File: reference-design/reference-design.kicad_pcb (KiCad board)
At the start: 2 copper layers, 12 x 20.6 mm, 21 parts

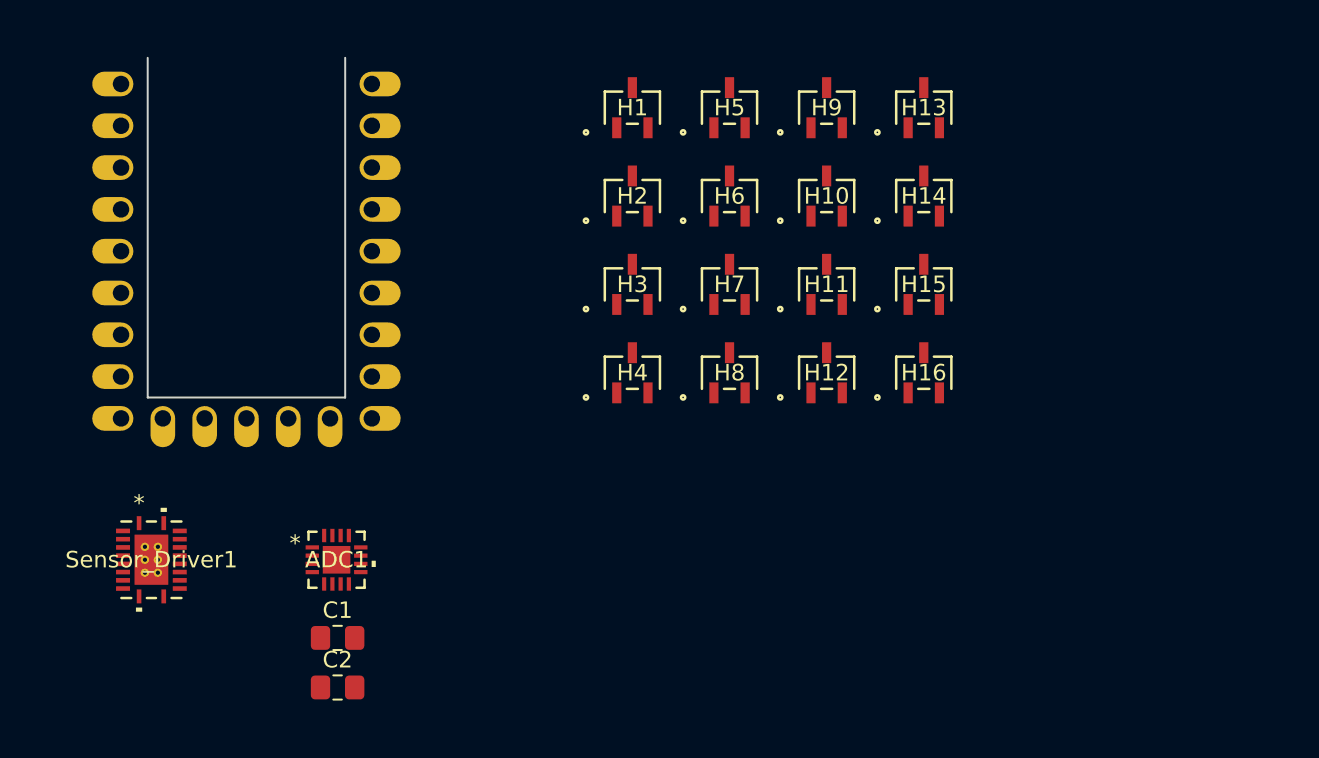
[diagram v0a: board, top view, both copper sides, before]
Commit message: associate 3d models for pcb preview
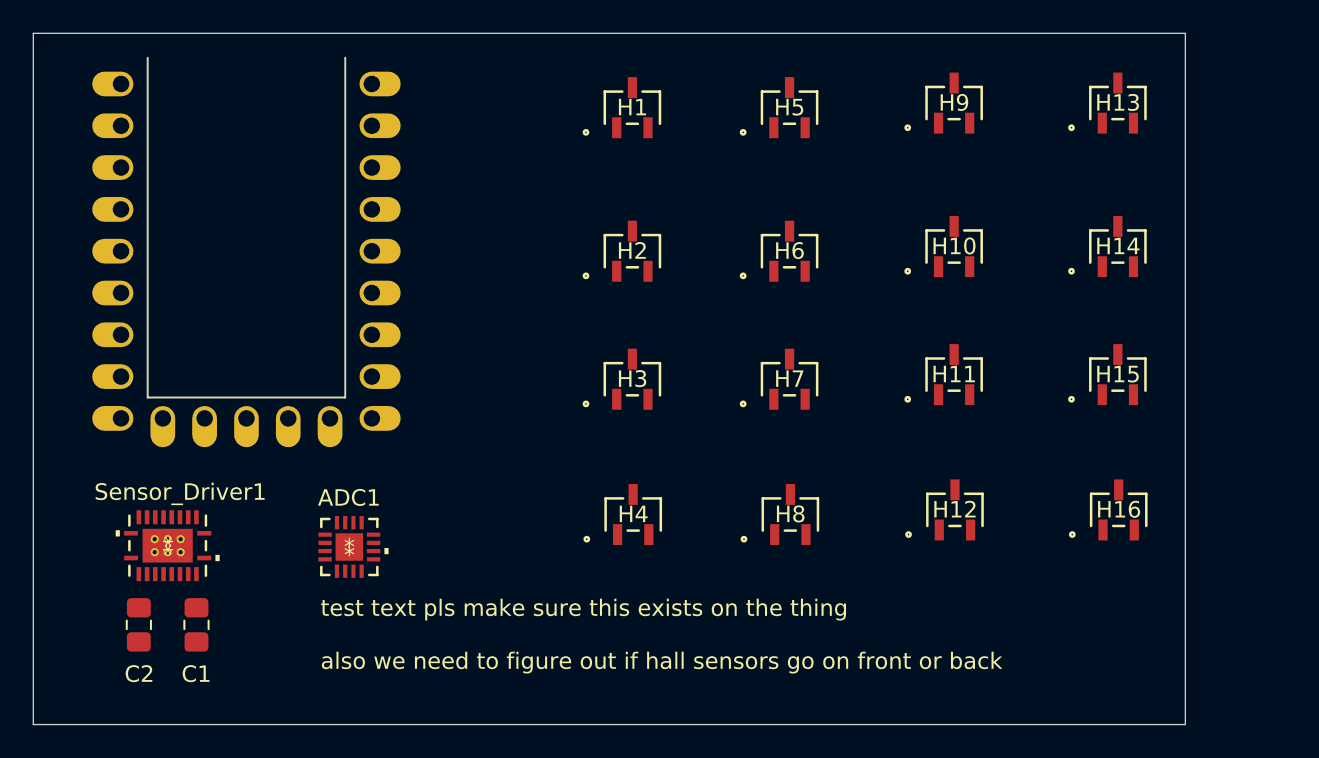
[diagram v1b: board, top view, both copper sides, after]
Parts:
- moved H16 14.5 mm to (78.5, 41.2)
- moved H15 13.0 mm to (78.5, 33.0)
- moved C2 12.7 mm to (19.0, 48.2), turned to 90 degrees
- moved H14 12.2 mm to (78.5, 25.2)
- moved H13 11.8 mm to (78.5, 16.5)
- moved H12 11.4 mm to (68.5, 41.2)
- moved H11 9.49 mm to (68.5, 33.0)
- moved H8 9.37 mm to (58.5, 41.5)
- moved H4 8.61 mm to (49.0, 41.5)
- moved C1 8.61 mm to (22.5, 48.2), turned to 90 degrees
- moved H10 8.33 mm to (68.5, 25.2)
- moved H9 7.75 mm to (68.5, 16.5)
- moved H7 6.82 mm to (58.5, 33.3)
- moved H3 5.76 mm to (49.0, 33.3)
- moved H6 4.95 mm to (58.5, 25.5)
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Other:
- board size 12 x 20.6 mm -> 70 x 42 mm
- board text added: "test text pls make sure this exists on the thing also we need to figure out if hall sensors go on front or back"

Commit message: SCH and PCB cleanup
- Ran ERC
- Added NCs to unused pins
- Fixed unconnected output pin on one of the sensors
- Cleaned up expected violations
- Rearranged sensors on PCB to match the pattern on the schematic
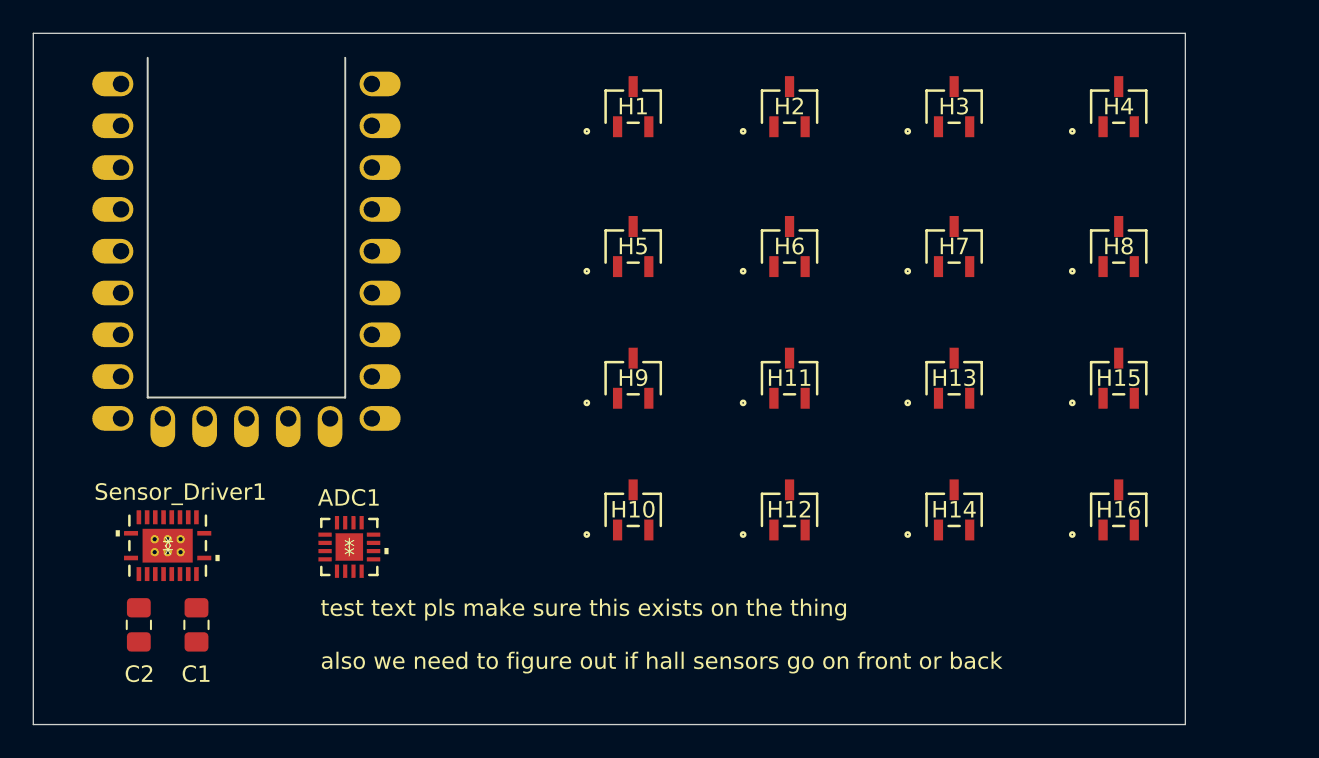
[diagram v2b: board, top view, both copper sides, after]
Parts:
- moved H4 38.5 mm to (78.5, 16.7)
- moved H8 25.8 mm to (78.5, 25.2)
- moved H9 25.7 mm to (49.0, 33.2)
- moved H3 25.6 mm to (68.5, 16.7)
- moved H10 25.2 mm to (49.0, 41.2)
- moved H13 19.5 mm to (68.5, 33.2)
- moved H14 18.8 mm to (68.5, 41.2)
- moved H2 13.0 mm to (58.5, 16.7)
- moved H7 12.8 mm to (68.5, 25.2)
- moved H5 12.7 mm to (49.0, 25.2)
- moved H12 10.0 mm to (58.5, 41.2)
- moved H11 10.0 mm to (58.5, 33.2)
- moved H6 0.28 mm to (58.5, 25.2)
- moved H15 0.22 mm to (78.5, 33.2)
- moved H1 0.08 mm to (49.0, 16.7)
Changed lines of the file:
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@@
 			(psa4output no)
 			(plot_black_and_white yes)
-			(plotinvisibletext no)
 			(sketchpadsonfab no)
 			(plotpadnumbers no)
@@
 	(footprint "AH49FNTR_G1:SC59_DIO"
 		(layer "F.Cu")
-		(at 49 41.5)
+		(at 78.5 16.7192)
 		(tags "AH49FNTR-G1 ")
 		(property "Reference" "H4"
@@
 	(footprint "AH49FNTR_G1:SC59_DIO"
 		(layer "F.Cu")
-		(at 58.5 33.2808)
+		(at 68.5 25.2192)
 		(tags "AH49FNTR-G1 ")
 		(property "Reference" "H7"
@@
 	(footprint "AH49FNTR_G1:SC59_DIO"
 		(layer "F.Cu")
-		(at 48.950001 16.7808)
+		(at 49 16.7192)
 		(tags "AH49FNTR-G1 ")
 		(property "Reference" "H1"
@@
 	(footprint "AH49FNTR_G1:SC59_DIO"
 		(layer "F.Cu")
-		(at 68.5 16.5)
+		(at 49 33.2192)
 		(tags "AH49FNTR-G1 ")
 		(property "Reference" "H9"
@@
 	(footprint "AH49FNTR_G1:SC59_DIO"
 		(layer "F.Cu")
-		(at 58.5 25.5)
+		(at 58.5 25.2192)
 		(tags "AH49FNTR-G1 ")
 		(property "Reference" "H6"
@@
 	(footprint "AH49FNTR_G1:SC59_DIO"
 		(layer "F.Cu")
-		(at 78.450001 16.5)
+		(at 68.5 33.2192)
 		(tags "AH49FNTR-G1 ")
 		(property "Reference" "H13"
@@
 	(footprint "AH49FNTR_G1:SC59_DIO"
 		(layer "F.Cu")
-		(at 68.549999 41.2192)
+		(at 58.5 41.2192)
 		(tags "AH49FNTR-G1 ")
 		(property "Reference" "H12"
@@
 	(footprint "AH49FNTR_G1:SC59_DIO"
 		(layer "F.Cu")
-		(at 48.950001 25.5)
+		(at 58.5 16.7192)
 		(tags "AH49FNTR-G1 ")
 		(property "Reference" "H2"
@@
 	(footprint "AH49FNTR_G1:SC59_DIO"
 		(layer "F.Cu")
-		(at 68.5 33)
+		(at 58.5 33.2192)
 		(tags "AH49FNTR-G1 ")
 		(property "Reference" "H11"
@@
 	(footprint "AH49FNTR_G1:SC59_DIO"
 		(layer "F.Cu")
-		(at 78.450001 25.2192)
+		(at 68.5 41.2192)
 		(tags "AH49FNTR-G1 ")
 		(property "Reference" "H14"
@@
 	(footprint "AH49FNTR_G1:SC59_DIO"
 		(layer "F.Cu")
-		(at 58.5 16.7808)
+		(at 49 25.2192)
 		(tags "AH49FNTR-G1 ")
 		(property "Reference" "H5"
@@
 	(footprint "AH49FNTR_G1:SC59_DIO"
 		(layer "F.Cu")
-		(at 78.450001 33)
+		(at 78.5 33.2192)
 		(tags "AH49FNTR-G1 ")
 		(property "Reference" "H15"
@@
 	(footprint "AH49FNTR_G1:SC59_DIO"
 		(layer "F.Cu")
-		(at 58.549999 41.5)
+		(at 78.5 25.2192)
 		(tags "AH49FNTR-G1 ")
 		(property "Reference" "H8"
@@
 	(footprint "AH49FNTR_G1:SC59_DIO"
 		(layer "F.Cu")
-		(at 48.950001 33.2808)
+		(at 68.5 16.7192)
 		(tags "AH49FNTR-G1 ")
 		(property "Reference" "H3"
@@
 	(footprint "AH49FNTR_G1:SC59_DIO"
 		(layer "F.Cu")
-		(at 68.5 25.2192)
+		(at 49 41.2192)
 		(tags "AH49FNTR-G1 ")
 		(property "Reference" "H10"
